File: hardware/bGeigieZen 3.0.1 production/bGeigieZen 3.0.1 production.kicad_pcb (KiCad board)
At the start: 2 copper layers, 129.4 x 64.6 mm, 17 parts, among them J1 M5 2x15 pin, J10 QI GND, J11 QI charger Plus, J2 Geiger IRover, J3 GPS, J4 Geiger Safepulse, J5 Extra support header, J6 Grove, J8 QI charger ground, J9 QI Plus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

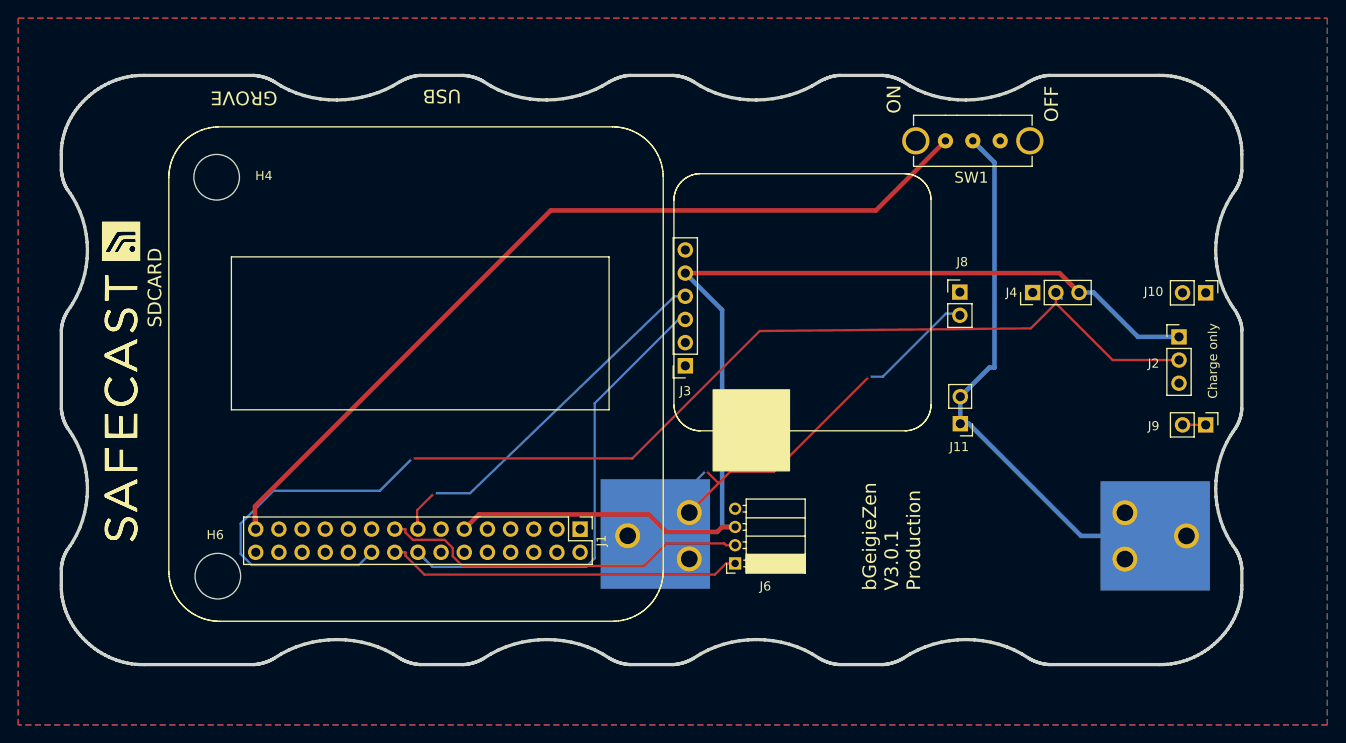
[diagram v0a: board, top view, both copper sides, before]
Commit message: Update Board to V3.0.2 (adjusted placement of the 4056)
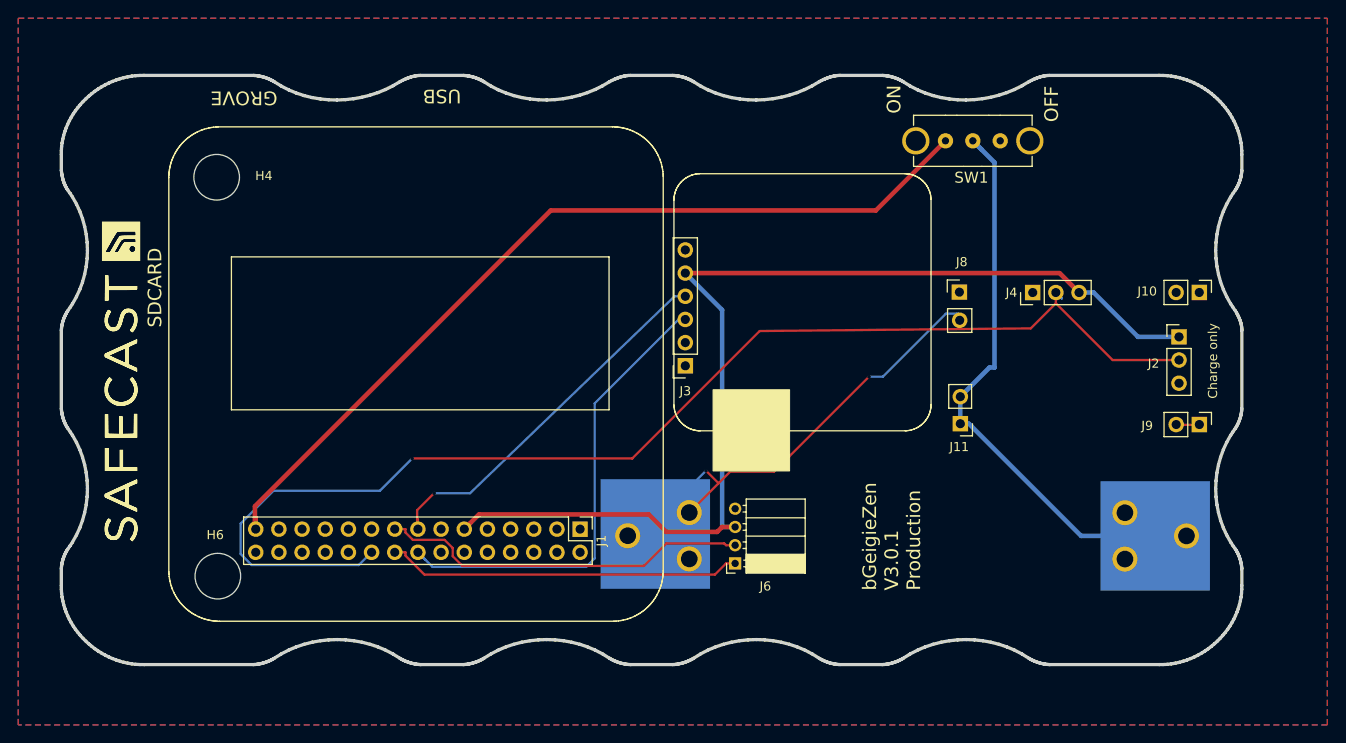
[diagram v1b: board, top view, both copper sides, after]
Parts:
- moved J9 0.70 mm to (209.3, 104.9)
- moved J10 0.70 mm to (209.3, 90.5)
- moved J8 0.05 mm to (183.0, 90.4)
